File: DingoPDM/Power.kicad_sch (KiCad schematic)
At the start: 12 parts, among them U1 VXO780x-500-M, U2 LD1117S33CTR

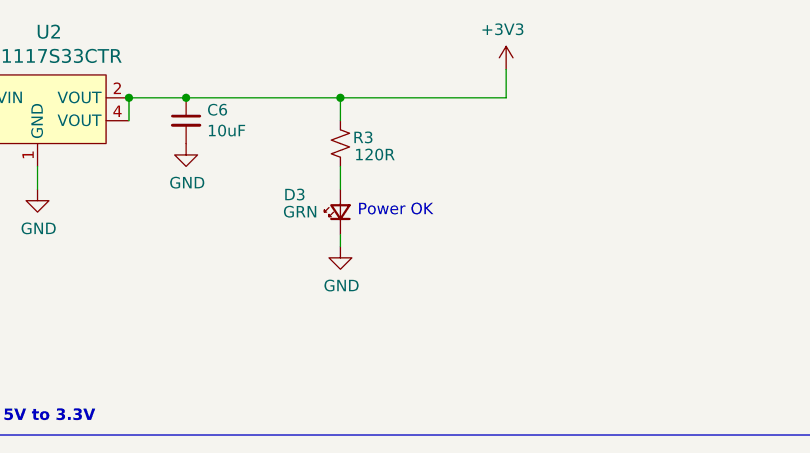
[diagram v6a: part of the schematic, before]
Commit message: Fixed USB, power LED and CAN standby
And increased screw hole size
#9, #11, #12, #13
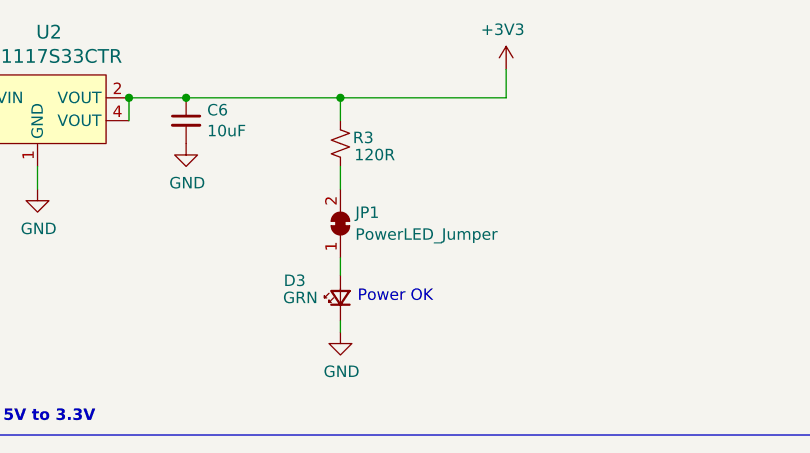
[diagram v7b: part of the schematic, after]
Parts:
- added JP1: PowerLED_Jumper, Jumper:SolderJumper-2_P1.3mm_Bridged_RoundedPad1.0x1.5mm, symbol Jumper:SolderJumper_2_Bridged
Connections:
- net at D3.2 (A): now also JP1.1 (A); no longer R3.1
- new net: JP1.2 (B), R3.1
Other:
- moved on the sheet: D3
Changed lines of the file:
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@@
   (title_block
     (title "Dingo_PDM")
-    (date "2023-09-11")
-    (rev "v7.2")
+    (date "2024-05-26")
+    (rev "v7.3")
     (comment 3 "github.com/corygrant")
     (comment 4 "Cory Grant")
@@
     (stroke (width 0) (type default))
   )
+  (wire (pts (xy 199.39 41.275) (xy 199.39 43.18))
+    (stroke (width 0) (type default))
+  )
   (wire (pts (xy 114.3 31.75) (xy 127.635 31.75))
     (stroke (width 0) (type default))
@@
     (stroke (width 0) (type default))
   )
-  (wire (pts (xy 199.39 40.005) (xy 199.39 38.735))
+  (wire (pts (xy 199.39 49.53) (xy 199.39 48.26))
     (stroke (width 0) (type default))
   )
@@
     (effects (font (size 1.27 1.27)) (justify left bottom))
   )
-  (text "Power OK" (at 201.295 36.83 0)
+  (text "Power OK" (at 201.295 46.355 0)
     (effects (font (size 1.27 1.27)) (justify left bottom))
   )
@@
     )
   )
-  (symbol (lib_id "Device:LED_Small") (at 199.39 36.195 90) (unit 1)
-    (in_bom yes) (on_board yes) (dnp no)
-    (property "Reference" "D3" (at 194.31 34.29 90)
-      (effects (font (size 1.27 1.27)))
-    )
-    (property "Value" "GRN" (at 194.945 36.195 90)
-      (effects (font (size 1.27 1.27)))
-    )
-    (property "Footprint" "LED_SMD:LED_0805_2012Metric" (at 199.39 36.195 90)
-      (effects (font (size 1.27 1.27)) hide)
-    )
-    (property "Datasheet" "" (at 199.39 36.195 90)
-      (effects (font (size 1.27 1.27)) hide)
-    )
-    (property "Digi-Key_PN" "475-1410-1-ND" (at 199.39 36.195 0)
-      (effects (font (size 1.27 1.27)) hide)
-    )
-    (property "LCSC" "C2899888" (at 199.39 36.195 0)
+  (symbol (lib_id "Device:LED_Small") (at 199.39 45.72 90) (unit 1)
+    (in_bom yes) (on_board yes) (dnp no)
+    (property "Reference" "D3" (at 194.31 43.815 90)
+      (effects (font (size 1.27 1.27)))
+    )
+    (property "Value" "GRN" (at 194.945 45.72 90)
+      (effects (font (size 1.27 1.27)))
+    )
+    (property "Footprint" "LED_SMD:LED_0805_2012Metric" (at 199.39 45.72 90)
+      (effects (font (size 1.27 1.27)) hide)
+    )
+    (property "Datasheet" "" (at 199.39 45.72 90)
+      (effects (font (size 1.27 1.27)) hide)
+    )
+    (property "Digi-Key_PN" "475-1410-1-ND" (at 199.39 45.72 0)
+      (effects (font (size 1.27 1.27)) hide)
+    )
+    (property "LCSC" "C2899888" (at 199.39 45.72 0)
       (effects (font (size 1.27 1.27)) hide)
     )
@@
     )
   )
-  (symbol (lib_id "power:GND") (at 199.39 40.005 0) (unit 1)
-    (in_bom yes) (on_board yes) (dnp no)
-    (property "Reference" "#PWR016" (at 199.39 46.355 0)
-      (effects (font (size 1.27 1.27)) hide)
-    )
-    (property "Value" "GND" (at 199.517 44.3992 0)
-      (effects (font (size 1.27 1.27)))
-    )
-    (property "Footprint" "" (at 199.39 40.005 0)
-      (effects (font (size 1.27 1.27)) hide)
-    )
-    (property "Datasheet" "" (at 199.39 40.005 0)
+  (symbol (lib_id "power:GND") (at 199.39 49.53 0) (unit 1)
+    (in_bom yes) (on_board yes) (dnp no)
+    (property "Reference" "#PWR016" (at 199.39 55.88 0)
+      (effects (font (size 1.27 1.27)) hide)
+    )
+    (property "Value" "GND" (at 199.517 53.9242 0)
+      (effects (font (size 1.27 1.27)))
+    )
+    (property "Footprint" "" (at 199.39 49.53 0)
+      (effects (font (size 1.27 1.27)) hide)
+    )
+    (property "Datasheet" "" (at 199.39 49.53 0)
       (effects (font (size 1.27 1.27)) hide)
     )
@@
         )
       )
+    )
+  )
+  (symbol (lib_id "Jumper:SolderJumper_2_Bridged") (at 199.39 37.465 90) (unit 1)
+    (in_bom yes) (on_board yes) (dnp no) (fields_autoplaced)
+    (property "Reference" "JP1" (at 201.041 36.2529 90)
+      (effects (font (size 1.27 1.27)) (justify right))
+    )
+    (property "Value" "PowerLED_Jumper" (at 201.041 38.6771 90)
+      (effects (font (size 1.27 1.27)) (justify right))
+    )
+    (property "Footprint" "Jumper:SolderJumper-2_P1.3mm_Bridged_RoundedPad1.0x1.5mm" (at 199.39 37.465 0)
+      (effects (font (size 1.27 1.27)) hide)
+    )
+    (property "Datasheet" "~" (at 199.39 37.465 0)
+      (effects (font (size 1.27 1.27)) hide)
+    )
+    (pin "1")
+    (pin "2")
+    (instances
+      (project "DingoPDM"
+        (path "/8948e307-9174-4227-9c28-3ff885e6e83d/00000000-0000-0000-0000-00005f5cf2eb"
+          (reference "JP1") (unit 1)
+        )
+      )

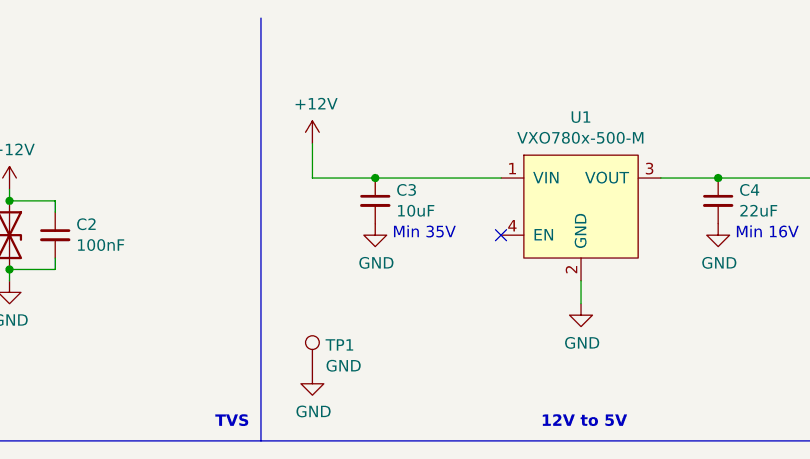
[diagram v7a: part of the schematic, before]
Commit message: Added diode for reverse battery protection
#14
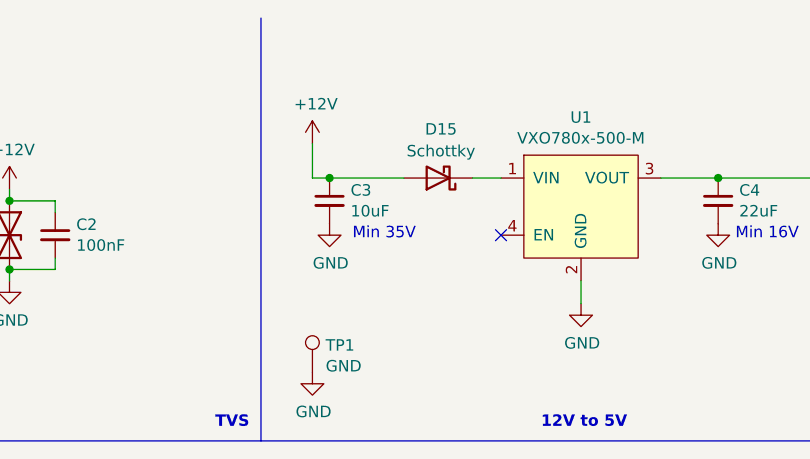
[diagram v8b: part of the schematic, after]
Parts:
- added D15: Schottky, Diode_SMD:D_SOD-123, symbol Device:D_Schottky
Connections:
- net +12V: now also D15.2 (A); no longer U1.1 (VIN)
- new net: D15.1 (K), U1.1 (VIN)
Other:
- moved on the sheet: C3
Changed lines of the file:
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@@
   (junction (at 114.3 31.75) (diameter 0) (color 0 0 0 0)
   )
+  (junction (at 71.12 31.75) (diameter 0) (color 0 0 0 0)
+  )
   (junction (at 149.225 23.495) (diameter 0) (color 0 0 0 0)
-  )
-  (junction (at 76.2 31.75) (diameter 0) (color 0 0 0 0)
   )
   (junction (at 35.56 34.29) (diameter 0) (color 0 0 0 0)
@@
     (stroke (width 0) (type default))
   )
+  (wire (pts (xy 86.995 31.75) (xy 90.17 31.75))
+    (stroke (width 0) (type default))
+  )
   (wire (pts (xy 199.39 31.115) (xy 199.39 33.655))
     (stroke (width 0) (type default))
@@
     (stroke (width 0) (type default))
   )
-  (wire (pts (xy 76.2 31.75) (xy 90.17 31.75))
+  (wire (pts (xy 71.12 31.75) (xy 79.375 31.75))
     (stroke (width 0) (type default))
   )
@@
     (stroke (width 0) (type default))
   )
-  (wire (pts (xy 69.215 31.75) (xy 76.2 31.75))
+  (wire (pts (xy 69.215 31.75) (xy 71.12 31.75))
     (stroke (width 0) (type default))
   )
@@
     (effects (font (size 1.27 1.27) (thickness 0.254) bold) (justify left bottom))
   )
-  (text "Min 35V" (at 78.105 38.735 0)
+  (text "Min 35V" (at 73.66 38.735 0)
     (effects (font (size 1.27 1.27)) (justify left bottom))
   )
@@
     )
   )
-  (symbol (lib_id "Device:C_Small") (at 76.2 34.29 0) (unit 1)
-    (in_bom yes) (on_board yes) (dnp no)
-    (property "Reference" "C3" (at 78.5368 33.1216 0)
-      (effects (font (size 1.27 1.27)) (justify left))
-    )
-    (property "Value" "10uF" (at 78.5368 35.433 0)
-      (effects (font (size 1.27 1.27)) (justify left))
-    )
-    (property "Footprint" "Capacitor_SMD:C_0805_2012Metric" (at 76.2 34.29 0)
-      (effects (font (size 1.27 1.27)) hide)
-    )
-    (property "Datasheet" "" (at 76.2 34.29 0)
-      (effects (font (size 1.27 1.27)) hide)
-    )
-    (property "Digi-Key_PN" "445-11516-1-ND" (at 76.2 34.29 0)
-      (effects (font (size 1.27 1.27)) hide)
-    )
-    (property "LCSC" "C15850" (at 76.2 34.29 0)
+  (symbol (lib_id "Device:C_Small") (at 71.12 34.29 0) (unit 1)
+    (in_bom yes) (on_board yes) (dnp no)
+    (property "Reference" "C3" (at 73.4568 33.1216 0)
+      (effects (font (size 1.27 1.27)) (justify left))
+    )
+    (property "Value" "10uF" (at 73.4568 35.433 0)
+      (effects (font (size 1.27 1.27)) (justify left))
+    )
+    (property "Footprint" "Capacitor_SMD:C_0805_2012Metric" (at 71.12 34.29 0)
+      (effects (font (size 1.27 1.27)) hide)
+    )
+    (property "Datasheet" "" (at 71.12 34.29 0)
+      (effects (font (size 1.27 1.27)) hide)
+    )
+    (property "Digi-Key_PN" "445-11516-1-ND" (at 71.12 34.29 0)
+      (effects (font (size 1.27 1.27)) hide)
+    )
+    (property "LCSC" "C15850" (at 71.12 34.29 0)
       (effects (font (size 1.27 1.27)) hide)
     )
@@
     )
   )
-  (symbol (lib_id "power:GND") (at 76.2 36.83 0) (unit 1)
-    (in_bom yes) (on_board yes) (dnp no)
-    (property "Reference" "#PWR09" (at 76.2 43.18 0)
-      (effects (font (size 1.27 1.27)) hide)
-    )
-    (property "Value" "GND" (at 76.327 41.2242 0)
-      (effects (font (size 1.27 1.27)))
-    )
-    (property "Footprint" "" (at 76.2 36.83 0)
-      (effects (font (size 1.27 1.27)) hide)
-    )
-    (property "Datasheet" "" (at 76.2 36.83 0)
+  (symbol (lib_id "power:GND") (at 71.12 36.83 0) (unit 1)
+    (in_bom yes) (on_board yes) (dnp no)
+    (property "Reference" "#PWR09" (at 71.12 43.18 0)
+      (effects (font (size 1.27 1.27)) hide)
+    )
+    (property "Value" "GND" (at 71.247 41.2242 0)
+      (effects (font (size 1.27 1.27)))
+    )
+    (property "Footprint" "" (at 71.12 36.83 0)
+      (effects (font (size 1.27 1.27)) hide)
+    )
+    (property "Datasheet" "" (at 71.12 36.83 0)
       (effects (font (size 1.27 1.27)) hide)
     )
@@
         )
       )
+    )
+  )
+  (symbol (lib_id "Device:D_Schottky") (at 83.185 31.75 180) (unit 1)
+    (in_bom yes) (on_board yes) (dnp no) (fields_autoplaced)
+    (property "Reference" "D15" (at 83.5025 26.3357 0)
+      (effects (font (size 1.27 1.27)))
+    )
+    (property "Value" "Schottky" (at 83.5025 28.7599 0)
+      (effects (font (size 1.27 1.27)))
+    )
+    (property "Footprint" "Diode_SMD:D_SOD-123" (at 83.185 31.75 0)
+      (effects (font (size 1.27 1.27)) hide)
+    )
+    (property "Datasheet" "" (at 83.185 31.75 0)
+      (effects (font (size 1.27 1.27)) hide)
+    )
+    (property "Digi-Key_PN" "1727-2394-1-ND" (at 83.185 31.75 0)
+      (effects (font (size 1.27 1.27)) hide)
+    )
+    (property "LCSC" "C179426" (at 83.185 31.75 0)
+      (effects (font (size 1.27 1.27)) hide)
+    )
+    (pin "1")
+    (pin "2")
+    (instances
+      (project "DingoPDM"
+        (path "/8948e307-9174-4227-9c28-3ff885e6e83d/00000000-0000-0000-0000-00005f5b308f"
+          (reference "D15") (unit 1)
+        )
+        (path "/8948e307-9174-4227-9c28-3ff885e6e83d/00000000-0000-0000-0000-00005f5cf2eb"
+          (reference "D19") (unit 1)
+        )
+      )
